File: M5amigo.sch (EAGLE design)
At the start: 2 parts, among them CN1 CON_PINHD-2X15, CN2 CON_PINHD-2X15

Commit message: better Pinout understanding !
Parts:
- CN1: value CON_PINHD-2X15 -> CON_PINHD-2X15_BOTTOM; device akita:CON_PINHD-2X15 -> akita:CON_PINHD-2X15_BOTTOM
- CN2: value CON_PINHD-2X15 -> CON_PINHD-2X15_TOP; device akita:CON_PINHD-2X15 -> akita:CON_PINHD-2X15_TOP
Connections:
- net 1: now also CN1.2; no longer CN1.1
- net 10: now also CN1.9; no longer CN1.10
- net 11: now also CN1.12; no longer CN1.11
- net 12: now also CN1.11; no longer CN1.12
- net 13: now also CN1.14; no longer CN1.13
- net 14: now also CN1.13; no longer CN1.14
- net 15: now also CN1.16; no longer CN1.15
- net 16: now also CN1.15; no longer CN1.16
- net 17: now also CN1.18; no longer CN1.17
- net 18: now also CN1.17; no longer CN1.18
- net 19: now also CN1.20; no longer CN1.19
- net 20: now also CN1.19; no longer CN1.20
- net 21: now also CN1.22; no longer CN1.21
- net 22: now also CN1.21; no longer CN1.22
- net 23: now also CN1.24; no longer CN1.23
- net 24: now also CN1.23; no longer CN1.24
- net 25: now also CN1.26; no longer CN1.25
- net 27: now also CN1.28; no longer CN1.27
- net 29: now also CN1.30; no longer CN1.29
- net 3: now also CN1.4; no longer CN1.3
- net 30: now also CN1.25, CN1.27, CN1.29; no longer CN1.26, CN1.28, CN1.30
- net 5: now also CN1.6; no longer CN1.5
- net 6: now also CN1.3, CN1.5, CN1.GND, CN2.GND; no longer CN1.2, CN1.4, CN1.6, CN2.1
- net 7: now also CN1.8; no longer CN1.7
- net 8: now also CN1.7; no longer CN1.8
- net 9: now also CN1.10; no longer CN1.9
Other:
- moved on the sheet: CN1, CN2

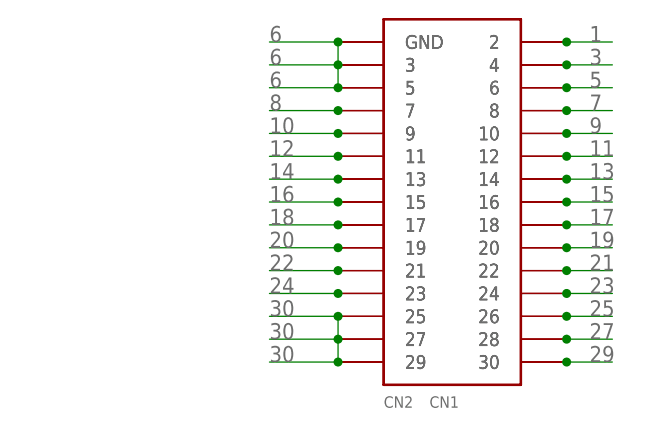
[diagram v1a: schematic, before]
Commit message: done. now it is more clear, the Pin-Cross is in the Symbol.
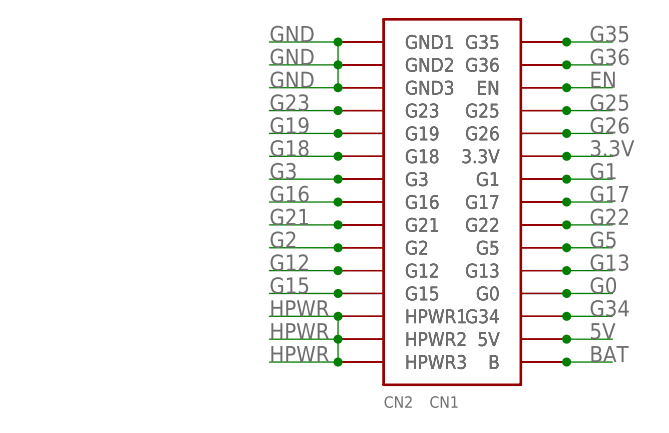
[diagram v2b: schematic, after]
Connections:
- removed net 1: CN1.2, CN2.2
- removed net 10: CN1.9, CN2.9
- removed net 11: CN1.12, CN2.12
- removed net 12: CN1.11, CN2.11
- removed net 13: CN1.14, CN2.14
- removed net 14: CN1.13, CN2.13
- removed net 15: CN1.16, CN2.16
- removed net 16: CN1.15, CN2.15
- removed net 17: CN1.18, CN2.18
- removed net 18: CN1.17, CN2.17
- removed net 19: CN1.20, CN2.20
- removed net 20: CN1.19, CN2.19
- removed net 21: CN1.22, CN2.22
- removed net 22: CN1.21, CN2.21
- removed net 23: CN1.24, CN2.24
- removed net 24: CN1.23, CN2.23
- removed net 25: CN1.26, CN2.26
- removed net 27: CN1.28, CN2.28
- removed net 29: CN1.30, CN2.30
- removed net 3: CN1.4, CN2.4
- removed net 30: CN1.25, CN1.27, CN1.29, CN2.25, CN2.27, CN2.29
- removed net 5: CN1.6, CN2.6
- removed net 6: CN1.3, CN1.5, CN1.GND, CN2.3, CN2.5, CN2.GND
- removed net 7: CN1.8, CN2.8
- removed net 8: CN1.7, CN2.7
- removed net 9: CN1.10, CN2.10
- new net 3.3V: CN1.3.3V, CN2.3.3V
- new net 5V: CN1.5V, CN2.5V
- new net BAT: CN1.B, CN2.B
- new net EN: CN1.EN, CN2.EN
- new net G0: CN1.G0, CN2.G0
- new net G1: CN1.G1, CN2.G1
- new net G12: CN1.G12, CN2.G12
- new net G13: CN1.G13, CN2.G13
- new net G15: CN1.G15, CN2.G15
- new net G16: CN1.G16, CN2.G16
- new net G17: CN1.G17, CN2.G17
- new net G18: CN1.G18, CN2.G18
- new net G19: CN1.G19, CN2.G19
- new net G2: CN1.G2, CN2.G2
- new net G21: CN1.G21, CN2.G21
- new net G22: CN1.G22, CN2.G22
- new net G23: CN1.G23, CN2.G23
- new net G25: CN1.G25, CN2.G25
- new net G26: CN1.G26, CN2.G26
- new net G3: CN1.G3, CN2.G3
- new net G34: CN1.G34, CN2.G34
- new net G35: CN1.G35, CN2.G35
- new net G36: CN1.G36, CN2.G36
- new net G5: CN1.G5, CN2.G5
- new net GND: CN1.GND1, CN1.GND2, CN1.GND3, CN2.GND1, CN2.GND2, CN2.GND3
- new net HPWR: CN1.HPWR1, CN1.HPWR2, CN1.HPWR3, CN2.HPWR1, CN2.HPWR2, CN2.HPWR3
